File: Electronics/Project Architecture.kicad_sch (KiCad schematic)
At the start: 8 parts

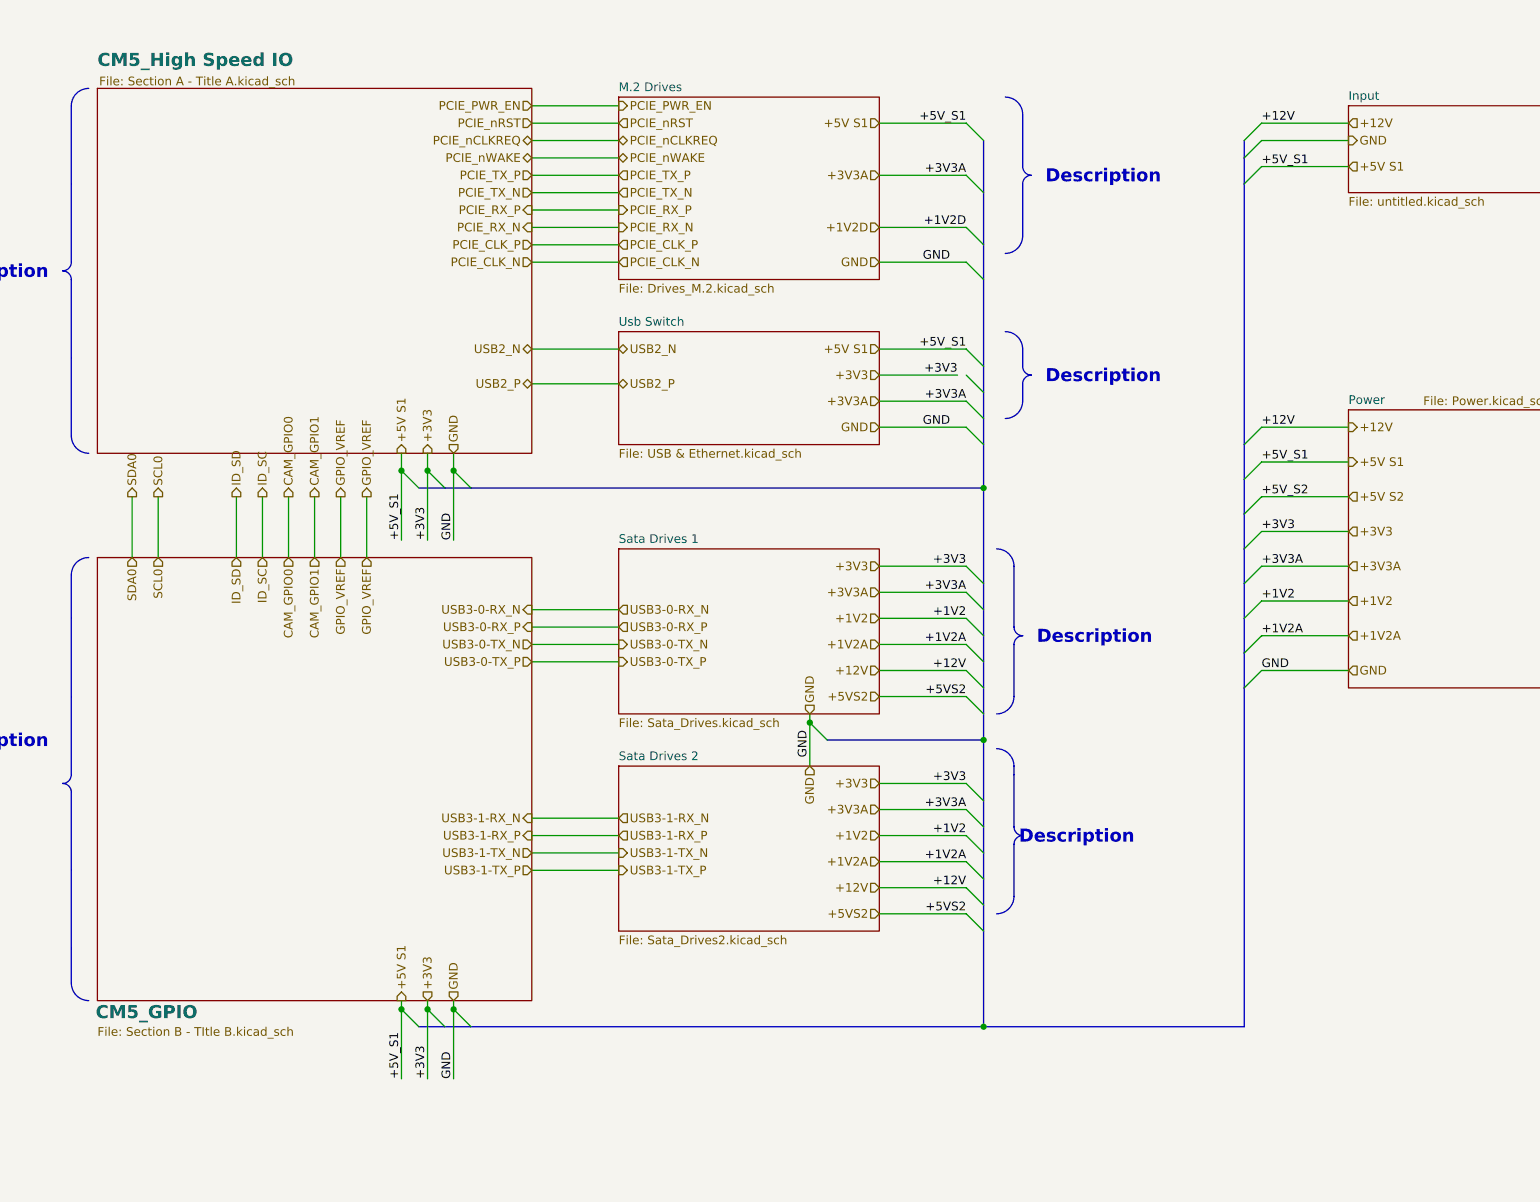
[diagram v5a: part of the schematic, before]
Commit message: Sata Port Changed
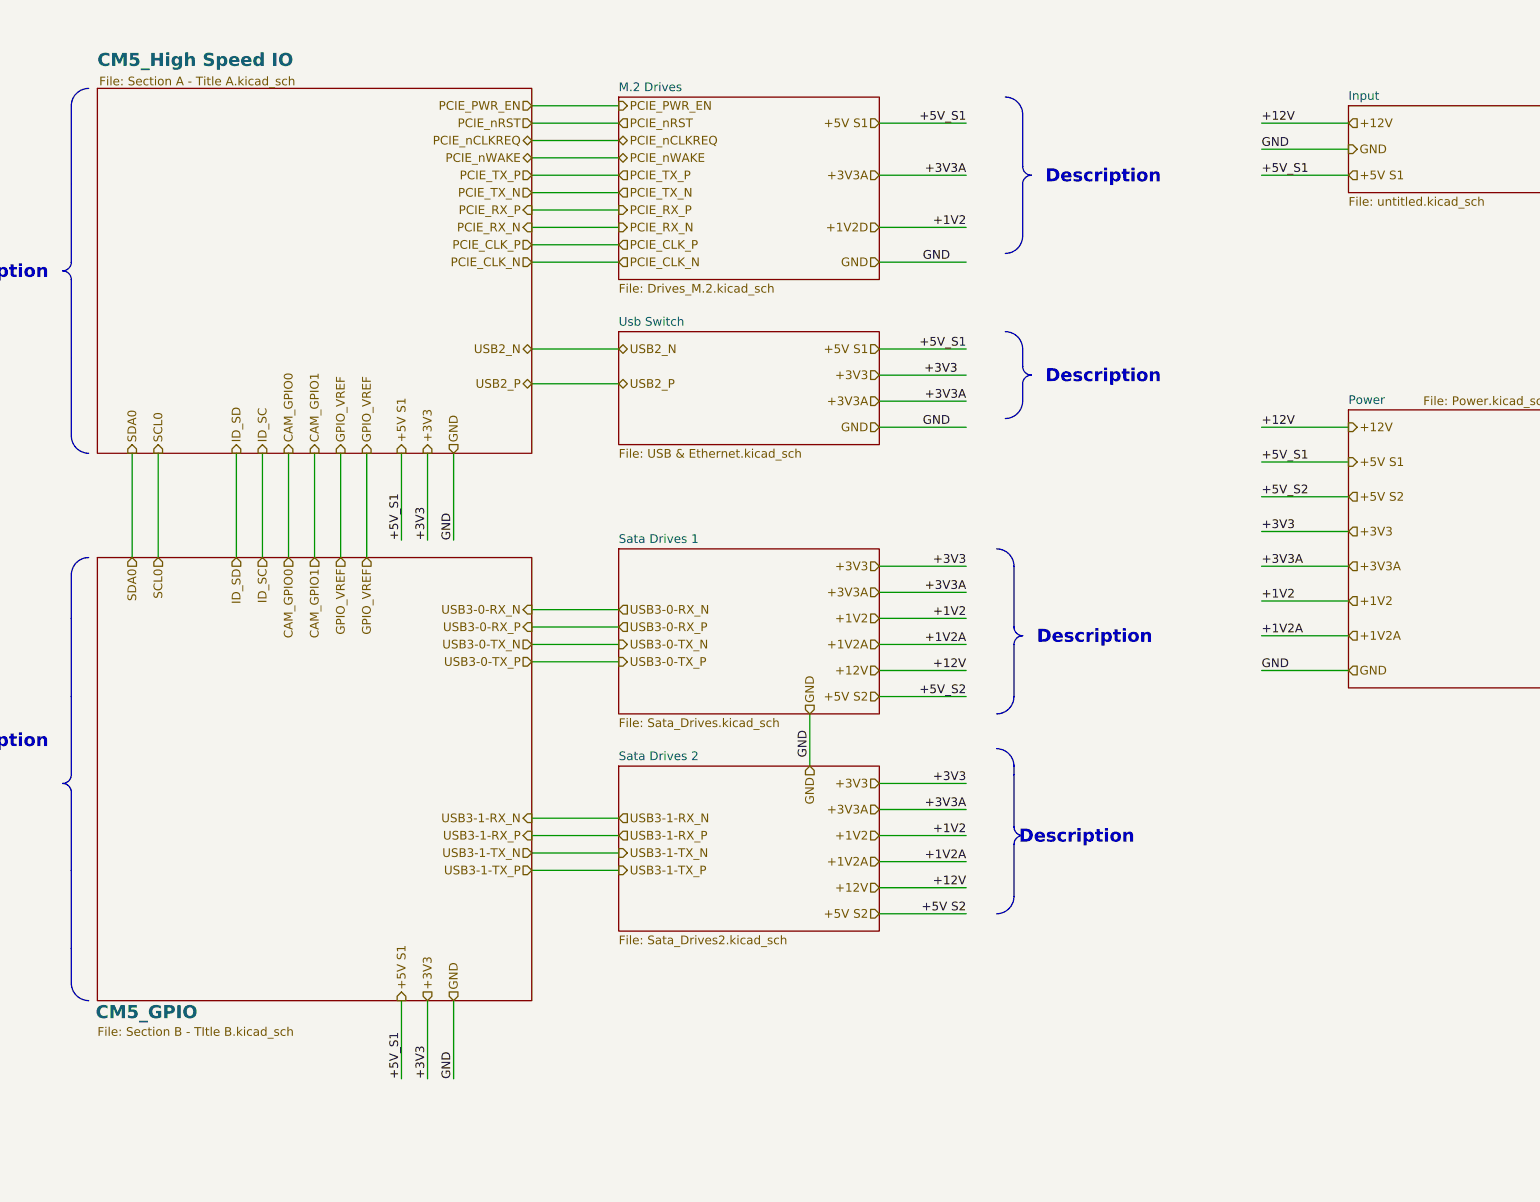
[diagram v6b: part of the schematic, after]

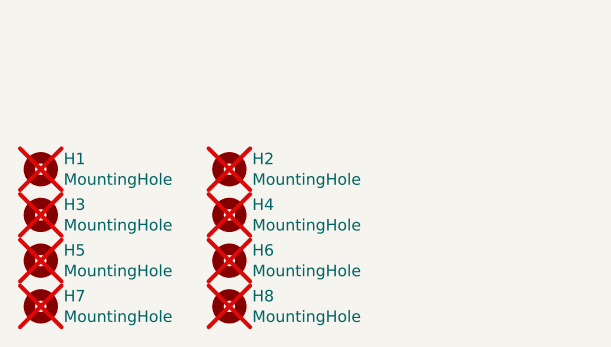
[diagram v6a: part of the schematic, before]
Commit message: Changed sata port
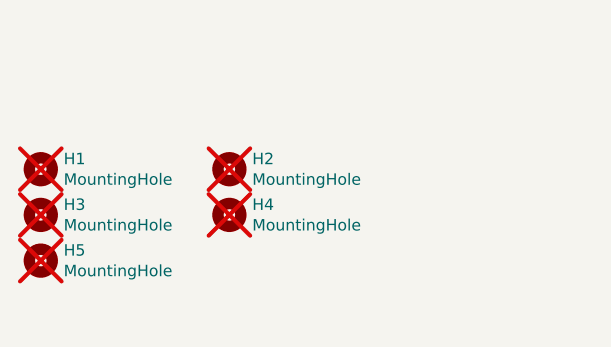
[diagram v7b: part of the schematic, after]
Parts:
- removed H6, H7, H8: MountingHole, MountingHole:MountingHole_2.7mm_M2.5, symbol Mechanical:MountingHole

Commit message: More pcbing
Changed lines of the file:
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@@
 	)
 	(hierarchical_label "PCIE_CLK_N"
-		(shape input)
+		(shape output)
 		(at 165.1 88.9 180)
 		(effects
@@
 	)
 	(hierarchical_label "PCIE_CLK_P"
-		(shape input)
+		(shape output)
 		(at 165.1 86.36 180)
 		(effects
@@
 			)
 			(justify right)
+		)
+	)
+	(rule_area
+		(polyline
+			(pts
+				(xy 105.41 119.38) (xy 105.41 129.54) (xy 111.76 129.54) (xy 111.76 119.38)
+			)
+			(stroke
+				(width 0)
+				(type dash)
+			)
+			(fill
+				(type none)
+			)
+		)
+	)
+	(rule_area
+		(polyline
+			(pts
+				(xy 167.64 90.17) (xy 175.26 90.17) (xy 175.26 74.93) (xy 167.64 74.93)
+			)
+			(stroke
+				(width 0)
+				(type dash)
+			)
+			(fill
+				(type none)
+			)
+		)
+	)
+	(rule_area
+		(polyline
+			(pts
+				(xy 281.94 149.86) (xy 271.78 149.86) (xy 271.78 110.49) (xy 281.94 110.49)
+			)
+			(stroke
+				(width 0)
+				(type dash)
+			)
+			(fill
+				(type none)
+			)
 		)
 	)
@@
 		(polyline
 			(pts
-				(xy 281.94 149.86) (xy 271.78 149.86) (xy 271.78 110.49) (xy 281.94 110.49)
+				(xy 167.64 138.43) (xy 175.26 138.43) (xy 175.26 179.07) (xy 167.64 179.07)
 			)
 			(stroke
-				(width 0)
-				(type dash)
-			)
-			(fill
-				(type none)
-			)
-		)
-	)
-	(rule_area
-		(polyline
-			(pts
-				(xy 167.64 138.43) (xy 175.26 138.43) (xy 175.26 179.07) (xy 167.64 179.07)
-			)
-			(stroke
-				(width 0)
-				(type dash)
-			)
-			(fill
-				(type none)
-			)
-		)
-	)
-	(rule_area
-		(polyline
-			(pts
-				(xy 105.41 119.38) (xy 105.41 129.54) (xy 111.76 129.54) (xy 111.76 119.38)
-			)
-			(stroke
-				(width 0)
-				(type dash)
-			)
-			(fill
-				(type none)
-			)
-		)
-	)
-	(rule_area
-		(polyline
-			(pts
-				(xy 167.64 90.17) (xy 175.26 90.17) (xy 175.26 74.93) (xy 167.64 74.93)
-			)
-			(stroke
